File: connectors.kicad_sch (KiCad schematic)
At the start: 4 parts, among them J1 Conn_01x04_Pin, J2 Conn_01x04_Pin, J3 Conn_01x09_Pin, J4 Conn_02x03_Odd_Even

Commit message: finish schema design
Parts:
- J1: renamed from J3; footprint (none) -> Connector_PinHeader_2.54mm:PinHeader_1x09_P2.54mm_Vertical
- J2: renamed from J1; footprint (none) -> Connector_PinHeader_2.54mm:PinHeader_1x04_P2.54mm_Vertical
- J3: renamed from J2; footprint (none) -> Connector_PinHeader_2.54mm:PinHeader_1x04_P2.54mm_Vertical
- J4: footprint (none) -> Connector_PinHeader_2.54mm:PinHeader_2x03_P2.54mm_Vertical_SMD
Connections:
- net D2: now reaches J1.1 (Pin_1)
- net D3: now reaches J1.2 (Pin_2)
- net D4: now reaches J1.3 (Pin_3)
- net D5: now reaches J1.4 (Pin_4)
- net D6: now reaches J1.5 (Pin_5)
- net D7: now reaches J1.6 (Pin_6)
- net D8: now reaches J1.7 (Pin_7)
- net GND: now reaches J1.8 (Pin_8)
- net GND: now also J2.1 (Pin_1), J3.1 (Pin_1), J4.6 (Pin_6)
- net VCC: now reaches J1.9 (Pin_9)
- net VCC: now also J2.2 (Pin_2), J3.2 (Pin_2), J4.2 (Pin_2)
- net SDA: now reaches J2.3 (Pin_3)
- net SCK: now reaches J2.4 (Pin_4)
- net SCK: now also J4.3 (Pin_3)
- net MISO: now reaches J4.1 (Pin_1)
- net MOSI: now reaches J4.4 (Pin_4)
- net RESET: now reaches J4.5 (Pin_5)
- net RX: now reaches J3.3 (Pin_3)
- net TX: now reaches J3.4 (Pin_4)
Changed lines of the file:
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@@
 		(company "${name}")
+	)
+	(hierarchical_label "TX"
+		(shape output)
+		(at 167.64 97.79 0)
+		(effects
+			(font
+				(size 1.27 1.27)
+			)
+			(justify left)
+		)
+	)
+	(hierarchical_label "D5"
+		(shape bidirectional)
+		(at 127 130.81 0)
+		(effects
+			(font
+				(size 1.27 1.27)
+			)
+			(justify left)
+		)
+	)
+	(hierarchical_label "GND"
+		(shape passive)
+		(at 171.45 130.81 0)
+		(effects
+			(font
+				(size 1.27 1.27)
+			)
+			(justify left)
+		)
+	)
+	(hierarchical_label "SDA"
+		(shape bidirectional)
+		(at 130.81 93.98 0)
+		(effects
+			(font
+				(size 1.27 1.27)
+			)
+			(justify left)
+		)
+	)
+	(hierarchical_label "RX"
+		(shape input)
+		(at 167.64 95.25 0)
+		(effects
+			(font
+				(size 1.27 1.27)
+			)
+			(justify left)
+		)
+	)
+	(hierarchical_label "D6"
+		(shape bidirectional)
+		(at 127 133.35 0)
+		(effects
+			(font
+				(size 1.27 1.27)
+			)
+			(justify left)
+		)
+	)
+	(hierarchical_label "VCC"
+		(shape passive)
+		(at 127 143.51 0)
+		(effects
+			(font
+				(size 1.27 1.27)
+			)
+			(justify left)
+		)
+	)
+	(hierarchical_label "VCC"
+		(shape passive)
+		(at 167.64 92.71 0)
+		(effects
+			(font
+				(size 1.27 1.27)
+			)
+			(justify left)
+		)
+	)
+	(hierarchical_label "D2"
+		(shape bidirectional)
+		(at 127 123.19 0)
+		(effects
+			(font
+				(size 1.27 1.27)
+			)
+			(justify left)
+		)
+	)
+	(hierarchical_label "MOSI"
+		(shape input)
+		(at 171.45 128.27 0)
+		(effects
+			(font
+				(size 1.27 1.27)
+			)
+			(justify left)
+		)
+	)
+	(hierarchical_label "SCK"
+		(shape passive)
+		(at 130.81 96.52 0)
+		(effects
+			(font
+				(size 1.27 1.27)
+			)
+			(justify left)
+		)
+	)
+	(hierarchical_label "D7"
+		(shape bidirectional)
+		(at 127 135.89 0)
+		(effects
+			(font
+				(size 1.27 1.27)
+			)
+			(justify left)
+		)
+	)
+	(hierarchical_label "VCC"
+		(shape passive)
+		(at 171.45 125.73 0)
+		(effects
+			(font
+				(size 1.27 1.27)
+			)
+			(justify left)
+		)
+	)
+	(hierarchical_label "GND"
+		(shape passive)
+		(at 167.64 90.17 0)
+		(effects
+			(font
+				(size 1.27 1.27)
+			)
+			(justify left)
+		)
+	)
+	(hierarchical_label "RESET"
+		(shape passive)
+		(at 158.75 130.81 180)
+		(effects
+			(font
+				(size 1.27 1.27)
+			)
+			(justify right)
+		)
+	)
+	(hierarchical_label "D4"
+		(shape bidirectional)
+		(at 127 128.27 0)
+		(effects
+			(font
+				(size 1.27 1.27)
+			)
+			(justify left)
+		)
+	)
+	(hierarchical_label "GND"
+		(shape passive)
+		(at 127 140.97 0)
+		(effects
+			(font
+				(size 1.27 1.27)
+			)
+			(justify left)
+		)
+	)
+	(hierarchical_label "VCC"
+		(shape passive)
+		(at 130.81 91.44 0)
+		(effects
+			(font
+				(size 1.27 1.27)
+			)
+			(justify left)
+		)
+	)
+	(hierarchical_label "D3"
+		(shape bidirectional)
+		(at 127 125.73 0)
+		(effects
+			(font
+				(size 1.27 1.27)
+			)
+			(justify left)
+		)
+	)
+	(hierarchical_label "GND"
+		(shape passive)
+		(at 130.81 88.9 0)
+		(effects
+			(font
+				(size 1.27 1.27)
+			)
+			(justify left)
+		)
+	)
+	(hierarchical_label "SCK"
+		(shape passive)
+		(at 158.75 128.27 180)
+		(effects
+			(font
+				(size 1.27 1.27)
+			)
+			(justify right)
+		)
+	)
+	(hierarchical_label "MISO"
+		(shape output)
+		(at 158.75 125.73 180)
+		(effects
+			(font
+				(size 1.27 1.27)
+			)
+			(justify right)
+		)
+	)
+	(hierarchical_label "D8"
+		(shape bidirectional)
+		(at 127 138.43 0)
+		(effects
+			(font
+				(size 1.27 1.27)
+			)
+			(justify left)
+		)
 	)
 	(symbol
@@
 		(on_board yes)
 		(dnp no)
-		(property "Reference" "J3"
+		(property "Reference" "J1"
 			(at 122.555 118.11 0)
 			(effects
@@
 			)
 		)
-		(property "Footprint" ""
+		(property "Footprint" "Connector_PinHeader_2.54mm:PinHeader_1x09_P2.54mm_Vertical"
 			(at 121.92 133.35 0)
 			(effects
@@
 			(project ""
 				(path "/c1519fa5-dbfa-43a9-bb02-bb0bfad7a63d/4d8d8f83-119a-4c18-a993-5670755e1933"
-					(reference "J3")
+					(reference "J1")
 					(unit 1)
 				)
@@
 		(on_board yes)
 		(dnp no)
-		(property "Reference" "J1"
+		(property "Reference" "J2"
 			(at 126.365 83.82 0)
 			(effects
@@
 			)
 		)
-		(property "Footprint" ""
+		(property "Footprint" "Connector_PinHeader_2.54mm:PinHeader_1x04_P2.54mm_Vertical"
 			(at 125.73 91.44 0)
 			(effects
@@
 			(project ""
 				(path "/c1519fa5-dbfa-43a9-bb02-bb0bfad7a63d/4d8d8f83-119a-4c18-a993-5670755e1933"
-					(reference "J1")
+					(reference "J2")
 					(unit 1)
 				)
@@
 			)
 		)
-		(property "Footprint" ""
+		(property "Footprint" "Connector_PinHeader_2.54mm:PinHeader_2x03_P2.54mm_Vertical_SMD"
 			(at 163.83 128.27 0)
 			(effects
@@
 		(on_board yes)
 		(dnp no)
-		(property "Reference" "J2"
+		(property "Reference" "J3"
 			(at 163.195 82.55 0)
 			(effects
@@
 			)
 		)
-		(property "Footprint" ""
+		(property "Footprint" "Connector_PinHeader_2.54mm:PinHeader_1x04_P2.54mm_Vertical"
 			(at 162.56 92.71 0)
 			(effects
@@
 			(project ""
 				(path "/c1519fa5-dbfa-43a9-bb02-bb0bfad7a63d/4d8d8f83-119a-4c18-a993-5670755e1933"
-					(reference "J2")
+					(reference "J3")
 					(unit 1)
 				)

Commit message: update conn_02x03 footprint
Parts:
- J4: footprint Connector_PinHeader_2.54mm:PinHeader_2x03_P2.54mm_Vertical_SMD -> Connector_PinHeader_2.54mm:PinHeader_2x03_P2.54mm_Vertical
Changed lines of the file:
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@@
 			)
 		)
-		(property "Footprint" "Connector_PinHeader_2.54mm:PinHeader_2x03_P2.54mm_Vertical_SMD"
+		(property "Footprint" "Connector_PinHeader_2.54mm:PinHeader_2x03_P2.54mm_Vertical"
 			(at 163.83 128.27 0)
 			(effects

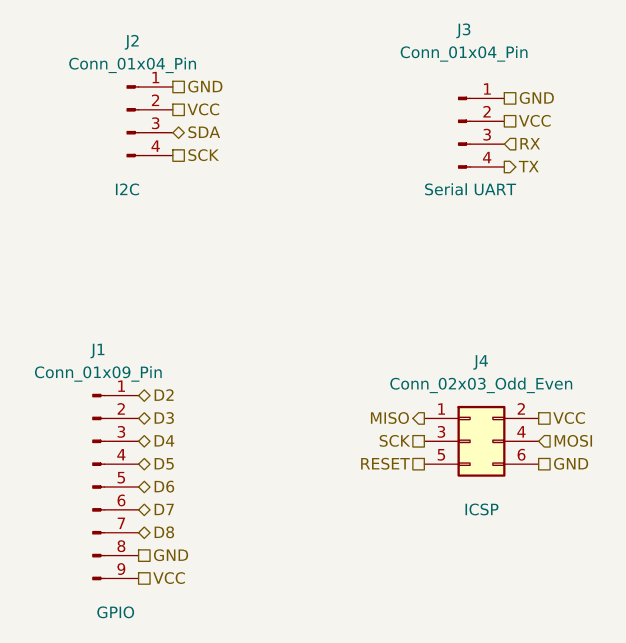
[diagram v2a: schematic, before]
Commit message: fix wrong SCL/SCK connection
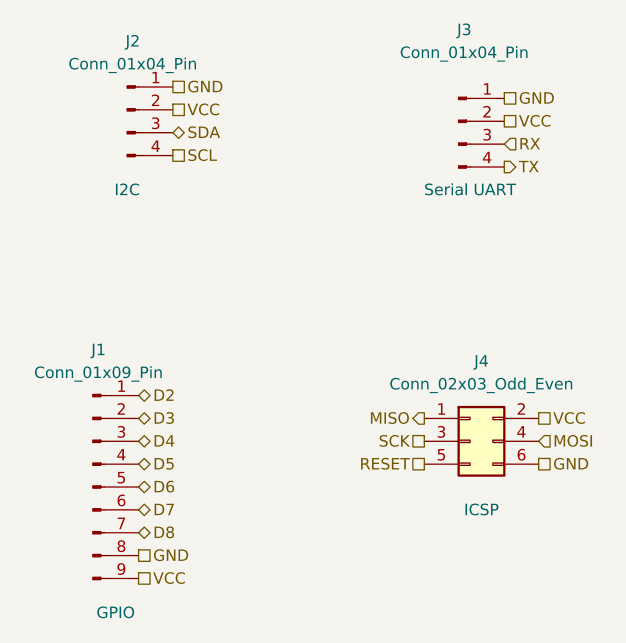
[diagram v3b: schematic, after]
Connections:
- net SCK: no longer J2.4 (Pin_4)
- new net SCL: J2.4 (Pin_4)
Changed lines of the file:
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@@
 		)
 	)
-	(hierarchical_label "SCK"
+	(hierarchical_label "SCL"
 		(shape passive)
 		(at 130.81 96.52 0)
